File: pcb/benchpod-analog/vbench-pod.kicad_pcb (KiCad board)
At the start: 4 copper layers, 98 x 118 mm, 248 parts, among them J8 Screw_Terminal_01x02, J9 Screw_Terminal_01x02, K1 G6K-2F-Y DC5, K2 G6K-2F-Y DC5, K3 G6K-2F-Y DC5, K4 G6K-2F-Y DC5, Q1 BCP56, U11 HX PZ2.54-1X2P ZZ, U12 HX PZ2.54-1X2P ZZ, U13 HX PZ2.54-1X2P ZZ, U14 HX PZ2.54-1X2P ZZ, U15 TPS7A2045PDBVR, U16 TLV61046ADBVR, U17 TMCP1A106MTRF, U3 TPS7A2050PDQNR, U30 TPS82130SILR, U36 MCP33131D-10-E/MS, U37 THS4551IRUNR, U38 ADR4540BRZ-R7, U39 AP2112K-1.8TRG1, U40 OPA810IDBVR, U41 LM27761DSGR, U42 LM7705MM/NOPB, U43 DAC8554IPWR, U44 OPA2365AIDR, U45 OPA2992IDR, U46 AP2112K-3.3, U49 TPS65131RGER, U50 TPS7A1901DRBR, U51 OPA2992IDR, U53 TPL7407LAPWR, U58 TCA9554PWR, U9 XTR116UA/2K5

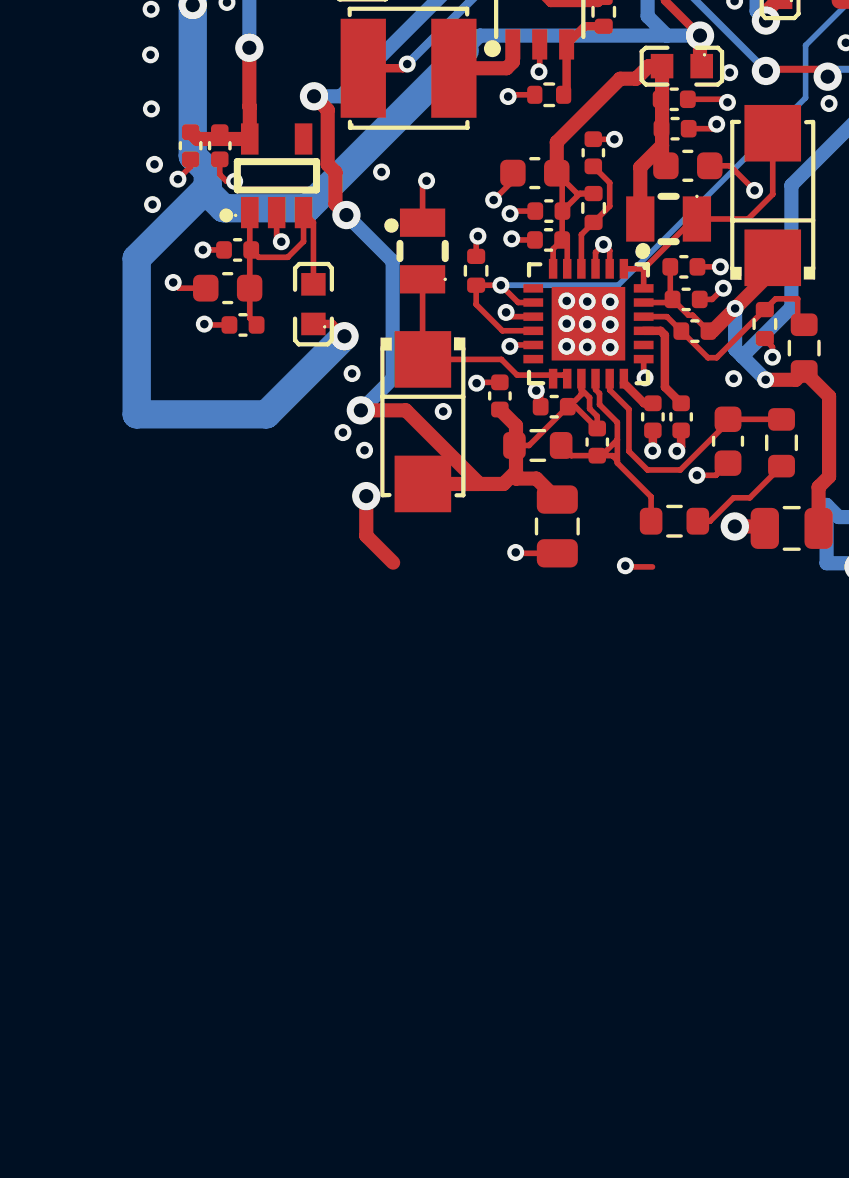
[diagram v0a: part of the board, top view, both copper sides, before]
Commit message: analog only board: CN1 FFC module link to the digital board
- CN1 KH-FPC1.0-H2.0SMT-24P-QCHF (C5123103), the same 24-pin 1.0 mm FFC
  connector as the digital board, on the root sheet. Pins 21-24 +5V,
  DAC_DIN/SCLK/SYNC, ADC_SDI/SCLK/SDO/CNVST and I2C0 to the existing labels;
  MOD_PRESENT# tied to GND; MOD_RESET# and MOD_SPARE unused; tabs to GND.
- Placed on the bottom side, under the digital CN1 (same X/Y from the
  top-left board corner), opening toward the left edge. Mounted upside down
  it is mirrored, so the pin order is reversed: pin N here = digital CN1
  pin 25-N (a flat cable keeps each wire at the same position). Text note on
  the sheet.
- PCB: only the footprint was added; it overlaps existing B.Cu routing
  (-14V_ANA, +5V, ANA14_EN, GND vias) that needs rerouting.

Co-Authored-By: Claude Opus 5.5 <noreply@anthropic.com>
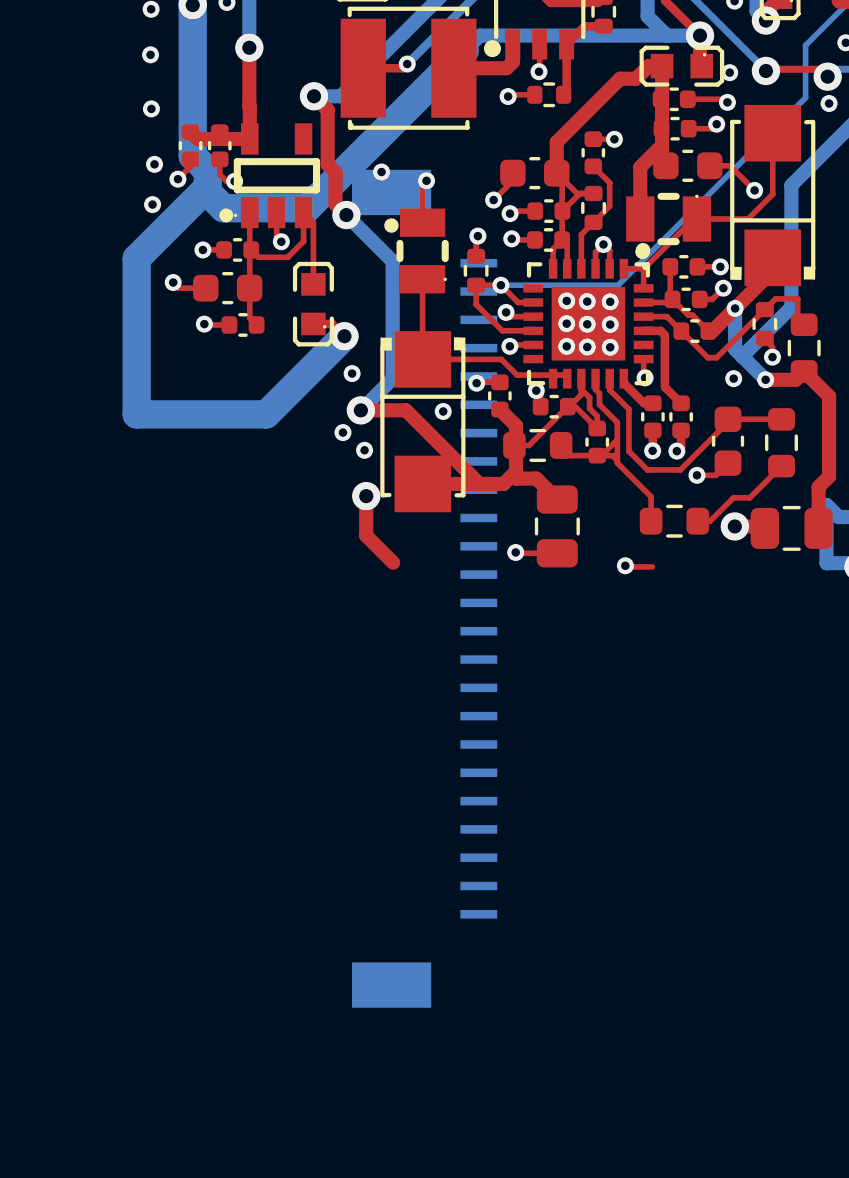
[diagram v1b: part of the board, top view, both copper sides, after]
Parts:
- added CN1: KH-FPC1.0-H2.0SMT-24P-QCHF, lcsc_footprints:C5123103_FPC-SMD_24P-P1.00_KH-FPC1.0-H2.0SMT-24P-QCHF, B.Cu at (55.0, 80.2)

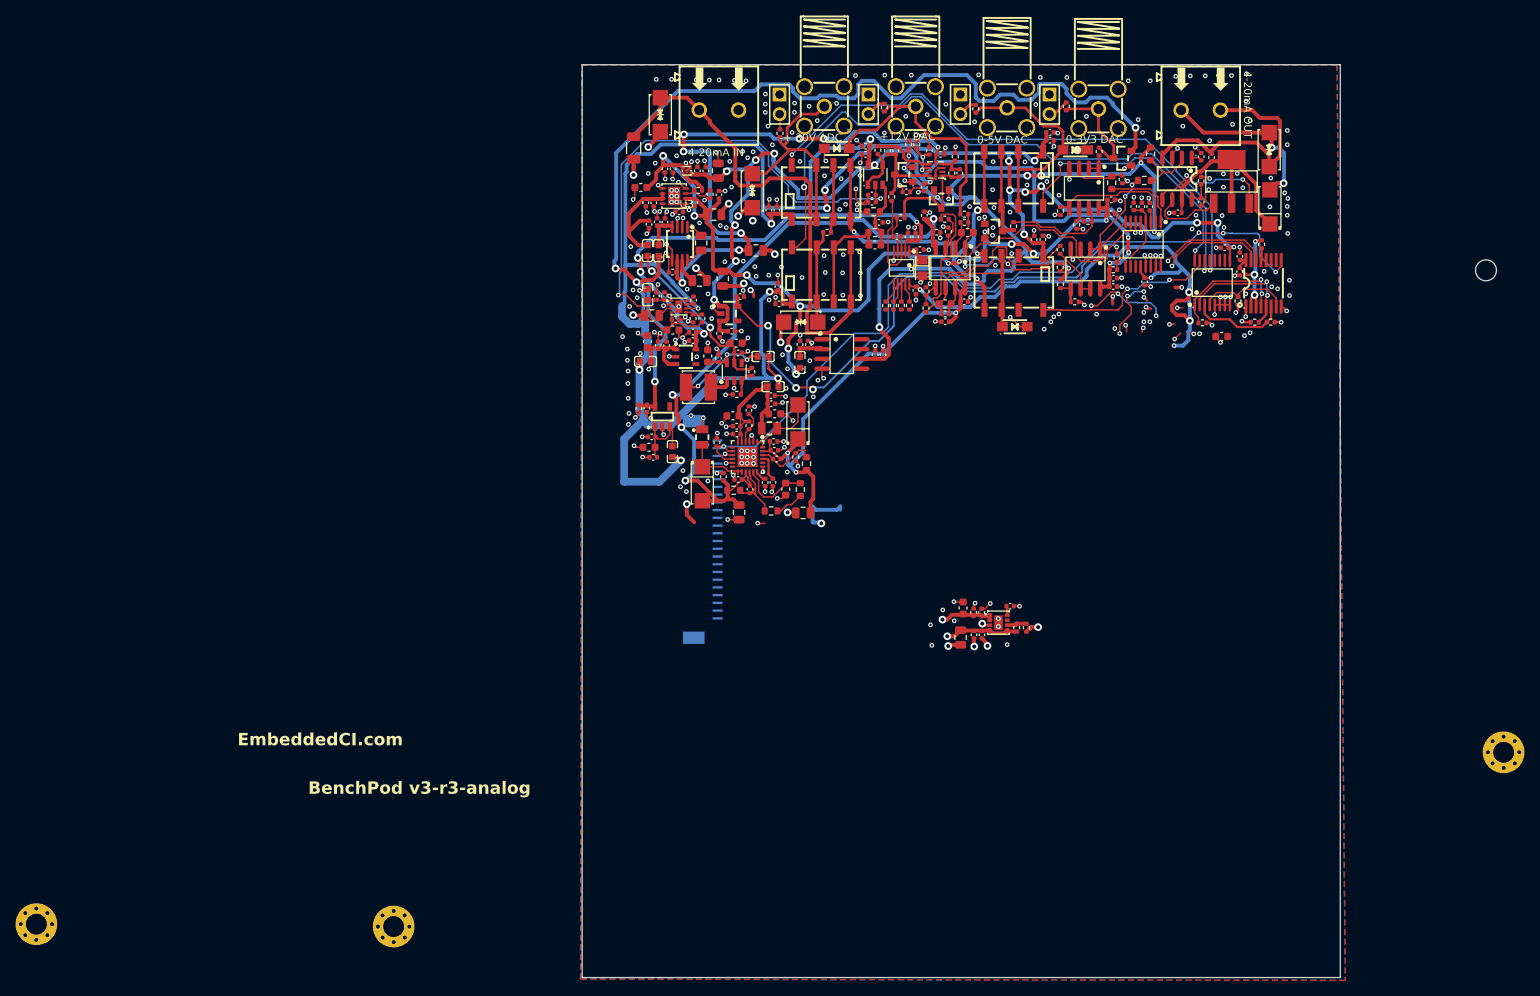
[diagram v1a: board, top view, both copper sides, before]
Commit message: analog only board: CN1 on the top side, straight pin order
The board now has a cut at the left edge for the FFC, so CN1 moves to the
top side with the same orientation as the digital CN1 (opening toward the
cut). The cable U-turns through the cut, so pin N = digital CN1 pin N again
(the reversed mapping is gone): pins 1-4 +5V, MOD_PRESENT# (21) to GND,
MOD_RESET# (20) and MOD_SPARE (23) unused. Note on the sheet updated.

PCB: CN1 on F.Cu, rotated -90, pin 1 at the digital pin-1 height (y 48.57
from the top edge), 2 mm further inboard (x 19.51) so the opening is about
3.3 mm from the cut's inner edge and the cable has room to bend.
Includes the board-edge cut drawn in KiCad.

Co-Authored-By: Claude Opus 5.5 <noreply@anthropic.com>
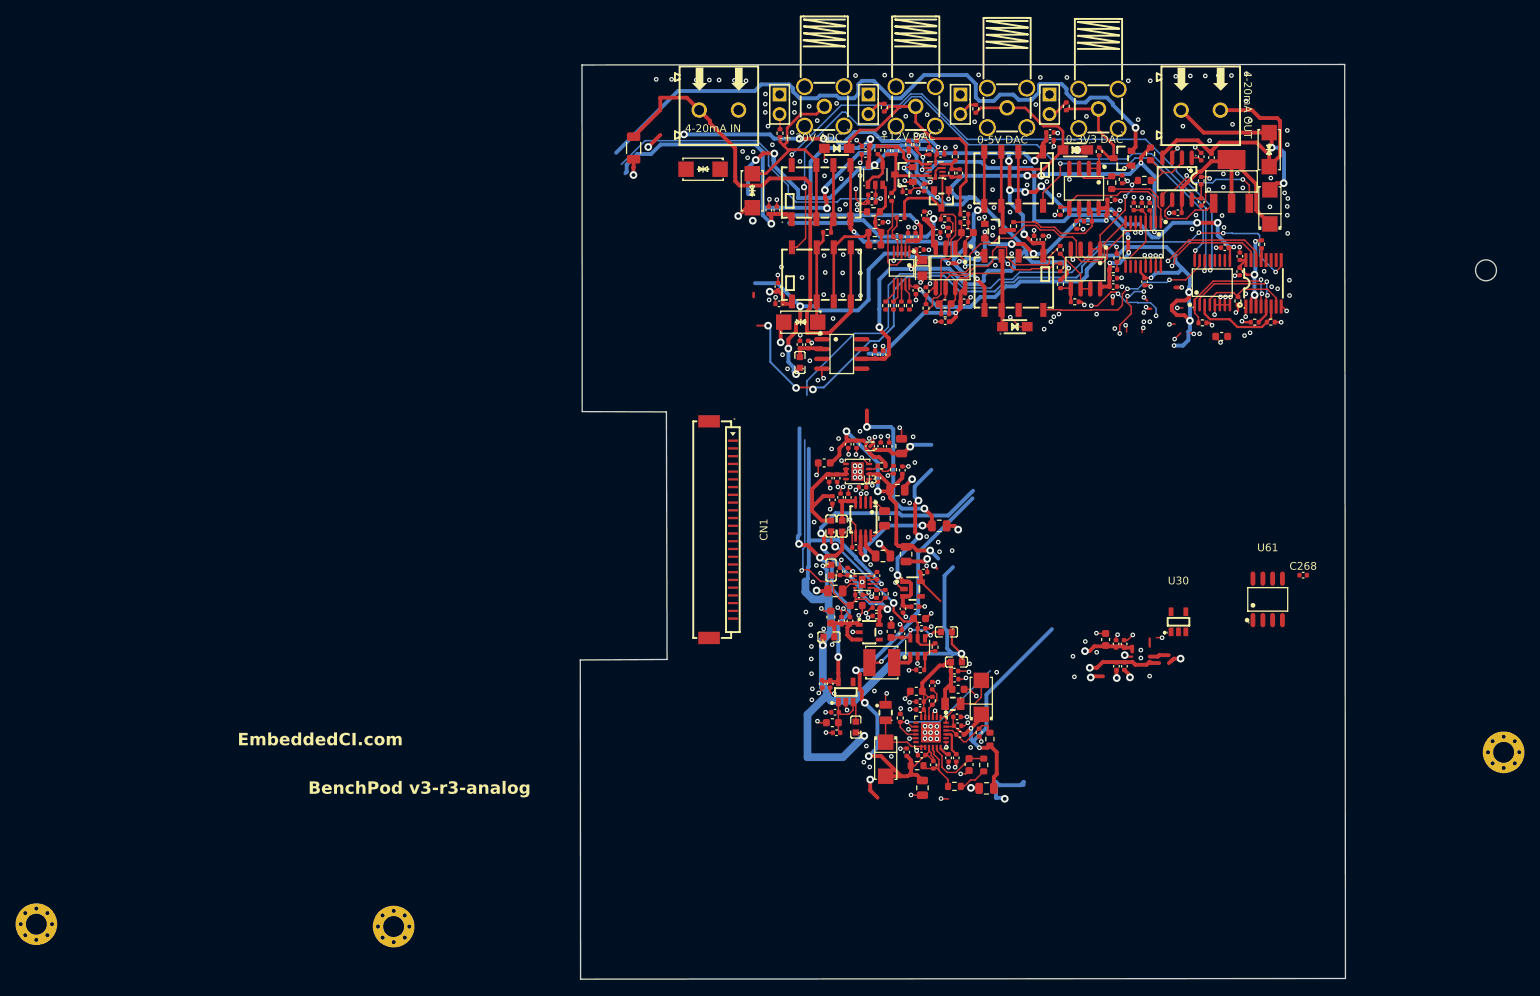
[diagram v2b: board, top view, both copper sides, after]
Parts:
- removed C108: 22u, Capacitor_SMD:C_0805_2012Metric
- removed C119: 3.3n, Capacitor_SMD:C_0402_1005Metric
- removed R85: 316k, Resistor_SMD:R_0402_1005Metric
- removed R86: 100k, Resistor_SMD:R_0402_1005Metric
- added C268: 100n, Capacitor_SMD:C_0402_1005Metric, F.Cu at (132.2, 86.1)
- added U61: 24C32, lcsc_footprints:C18723546_SOP-8_L4.9-W3.9-P1.27-LS6.0-BL, F.Cu at (127.6, 89.3)
- CN1: moved to F.Cu
- U30: value TPS82130SILR -> AP2112K-3.3; footprint lcsc:USIP-8_L3.0-W2.8-P0.65-TL-EP -> lcsc:SOT-25-5_L2.9-W1.6-P0.95-LS2.8-BL
- moved C173 42.8 mm to (70.1, 100.2)
- moved C174 42.8 mm to (71.1, 100.2)
- moved C127 42.8 mm to (72.5, 92.0)
- moved C129 42.8 mm to (73.6, 92.0)
- moved C196 42.8 mm to (80.9, 83.4)
- moved C248 42.8 mm to (74.5, 69.2)
- moved C261 42.8 mm to (80.3, 93.7)
- moved C264 42.8 mm to (82.9, 93.0)
- moved FB11 42.8 mm to (72.6, 79.8)
- moved R105 42.8 mm to (77.1, 88.6)
- moved R120 42.8 mm to (79.3, 72.5)
- moved U41 42.8 mm to (75.2, 87.0)
- moved C137 42.8 mm to (77.0, 90.3)
- moved C138 42.8 mm to (77.0, 91.4)
- moved C145 42.8 mm to (72.3, 85.7)
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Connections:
- CN1 pad 1: GND -> +5V
- CN1 pad 10: /ADC_CNVST -> GND
- CN1 pad 11: GND -> /ADC_SDI
- CN1 pad 12: /ADC_SDO -> /ADC_SCLK
- CN1 pad 13: /ADC_SCLK -> /ADC_SDO
- CN1 pad 14: /ADC_SDI -> GND
- CN1 pad 15: GND -> /ADC_CNVST
- CN1 pad 16: /DAC_SYNC -> GND
- CN1 pad 17: /DAC_SCLK -> /I2C0_SDA
- CN1 pad 18: /DAC_DIN -> /I2C0_SCL
- CN1 pad 2: unconnected-(CN1-Pad2) -> +5V
- CN1 pad 20: GND -> unconnected-(CN1-Pad20)
- CN1 pad 21: +5V -> GND
- CN1 pad 22: +5V -> GND
- CN1 pad 23: +5V -> unconnected-(CN1-Pad23)
- CN1 pad 24: +5V -> GND
- CN1 pad 3: GND -> +5V
- CN1 pad 4: GND -> +5V
- CN1 pad 5: unconnected-(CN1-Pad5) -> GND
- CN1 pad 7: /I2C0_SCL -> /DAC_DIN
- CN1 pad 8: /I2C0_SDA -> /DAC_SCLK
- CN1 pad 9: GND -> /DAC_SYNC
- U30 pad 2: +5V -> GND
- U30 pad 3: GND -> +5V
- U30 pad 4: +3V3 -> unconnected-(U30-NC-Pad4)
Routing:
- net unconnected-(U30-NC-Pad4): track 0.00 -> 1.06 mm
- net Net-(U30-SS/TR): track 1.06 -> 0.00 mm
- removed copper zone on B.Cu, net GND
- removed copper zone on F.Cu, net GND
- removed copper zone on In1.Cu, net GND
- removed copper zone on In2.Cu, net GND
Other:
- board size 98 x 118 mm -> 98.9 x 118.2 mm
